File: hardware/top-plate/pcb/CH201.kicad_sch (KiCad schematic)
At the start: 35 parts

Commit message: some top plate changes
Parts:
- C10, C7, C8, C9: footprint PCM_Capacitor_SMD_AKL:C_1206_3216Metric_Pad1.33x1.80mm_HandSolder -> PCM_Capacitor_SMD_AKL:C_0805_2012Metric_Pad1.15x1.40mm_HandSolder
- R1, R2, R3, R7, R8: footprint PCM_Resistor_SMD_AKL:R_1206_3216Metric_Pad1.30x1.75mm_HandSolder -> PCM_Resistor_SMD_AKL:R_0805_2012Metric_Pad1.15x1.40mm_HandSolder
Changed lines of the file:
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@@
 			)
 		)
-		(property "Footprint" "PCM_Resistor_SMD_AKL:R_1206_3216Metric_Pad1.30x1.75mm_HandSolder"
+		(property "Footprint" "PCM_Resistor_SMD_AKL:R_0805_2012Metric_Pad1.15x1.40mm_HandSolder"
 			(at 264.922 207.01 90)
 			(effects
@@
 			)
 		)
-		(property "Footprint" "PCM_Resistor_SMD_AKL:R_1206_3216Metric_Pad1.30x1.75mm_HandSolder"
+		(property "Footprint" "PCM_Resistor_SMD_AKL:R_0805_2012Metric_Pad1.15x1.40mm_HandSolder"
 			(at 209.042 207.01 90)
 			(effects
@@
 			)
 		)
-		(property "Footprint" "PCM_Capacitor_SMD_AKL:C_1206_3216Metric_Pad1.33x1.80mm_HandSolder"
+		(property "Footprint" "PCM_Capacitor_SMD_AKL:C_0805_2012Metric_Pad1.15x1.40mm_HandSolder"
 			(at 224.79 200.9648 0)
 			(effects
@@
 			)
 		)
-		(property "Footprint" "PCM_Capacitor_SMD_AKL:C_1206_3216Metric_Pad1.33x1.80mm_HandSolder"
+		(property "Footprint" "PCM_Capacitor_SMD_AKL:C_0805_2012Metric_Pad1.15x1.40mm_HandSolder"
 			(at 240.03 200.9648 0)
 			(effects
@@
 			)
 		)
-		(property "Footprint" "PCM_Capacitor_SMD_AKL:C_1206_3216Metric_Pad1.33x1.80mm_HandSolder"
+		(property "Footprint" "PCM_Capacitor_SMD_AKL:C_0805_2012Metric_Pad1.15x1.40mm_HandSolder"
 			(at 280.67 200.9648 0)
 			(effects
@@
 	)
 	(symbol
+		(lib_name "MCP23S17_SO_1")
 		(lib_id "Interface_Expansion:MCP23S17_SO")
 		(at 260.35 71.12 0)
@@
 			)
 		)
-		(property "Footprint" "PCM_Capacitor_SMD_AKL:C_1206_3216Metric_Pad1.33x1.80mm_HandSolder"
+		(property "Footprint" "PCM_Capacitor_SMD_AKL:C_0805_2012Metric_Pad1.15x1.40mm_HandSolder"
 			(at 295.91 200.9648 0)
 			(effects
@@
 			)
 		)
-		(property "Footprint" "PCM_Resistor_SMD_AKL:R_1206_3216Metric_Pad1.30x1.75mm_HandSolder"
+		(property "Footprint" "PCM_Resistor_SMD_AKL:R_0805_2012Metric_Pad1.15x1.40mm_HandSolder"
 			(at 182.372 245.11 90)
 			(effects
@@
 			)
 		)
-		(property "Footprint" "PCM_Resistor_SMD_AKL:R_1206_3216Metric_Pad1.30x1.75mm_HandSolder"
+		(property "Footprint" "PCM_Resistor_SMD_AKL:R_0805_2012Metric_Pad1.15x1.40mm_HandSolder"
 			(at 202.692 245.11 90)
 			(effects
@@
 			)
 		)
-		(property "Footprint" "PCM_Resistor_SMD_AKL:R_1206_3216Metric_Pad1.30x1.75mm_HandSolder"
+		(property "Footprint" "PCM_Resistor_SMD_AKL:R_0805_2012Metric_Pad1.15x1.40mm_HandSolder"
 			(at 192.532 245.11 90)
 			(effects

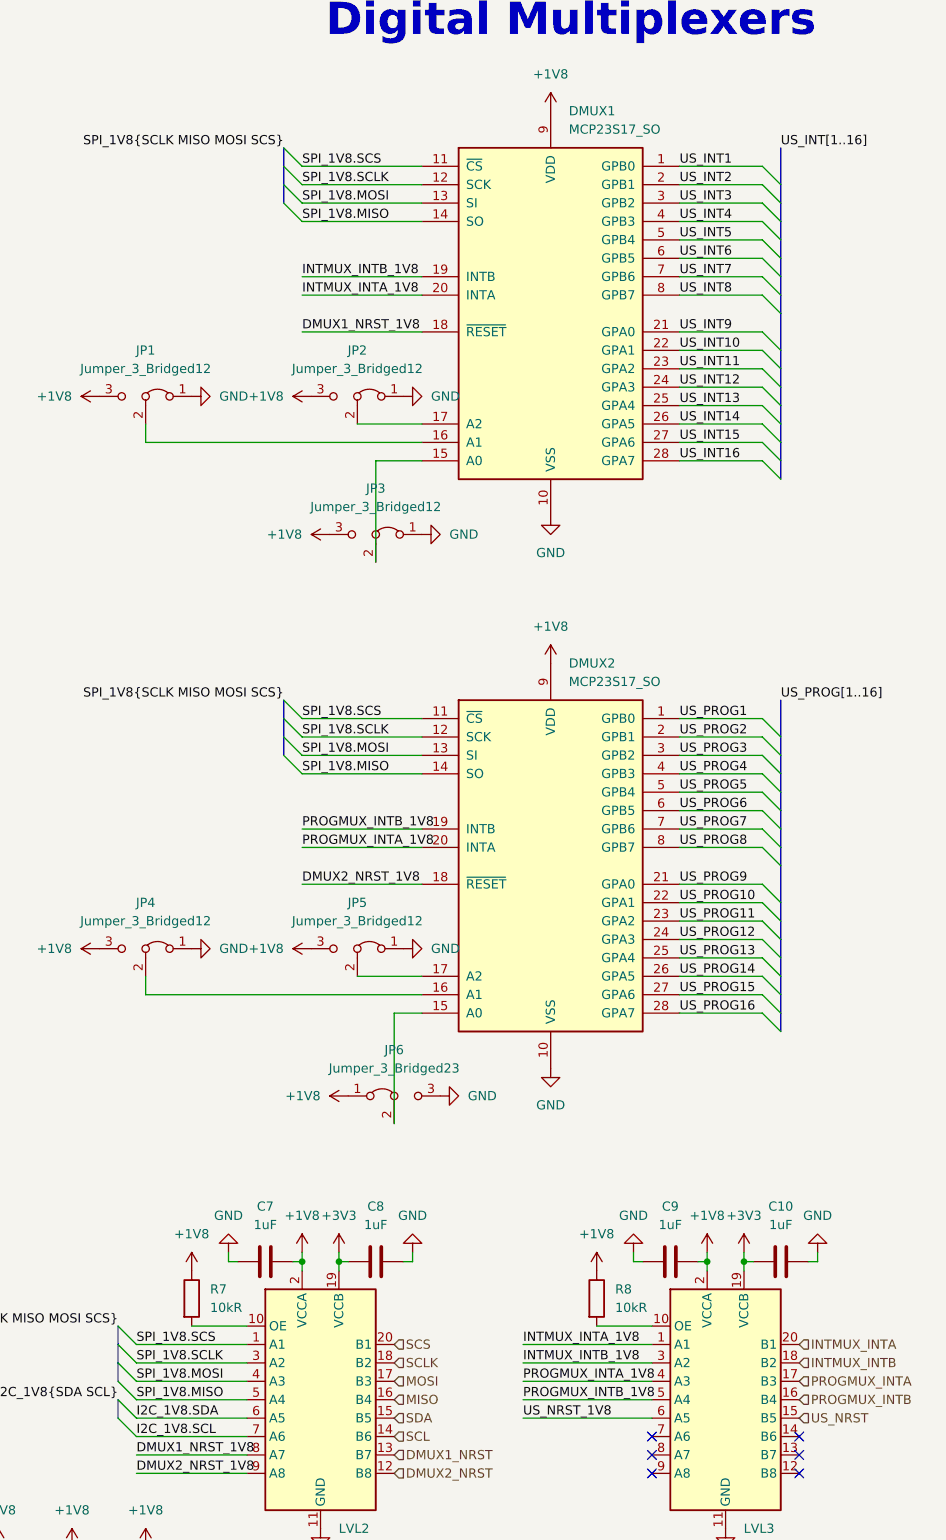
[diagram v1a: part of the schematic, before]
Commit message: fixed up bottom plate schematic. do not run a global symbol update! all modified symbols as of now are intentionally modified locally.
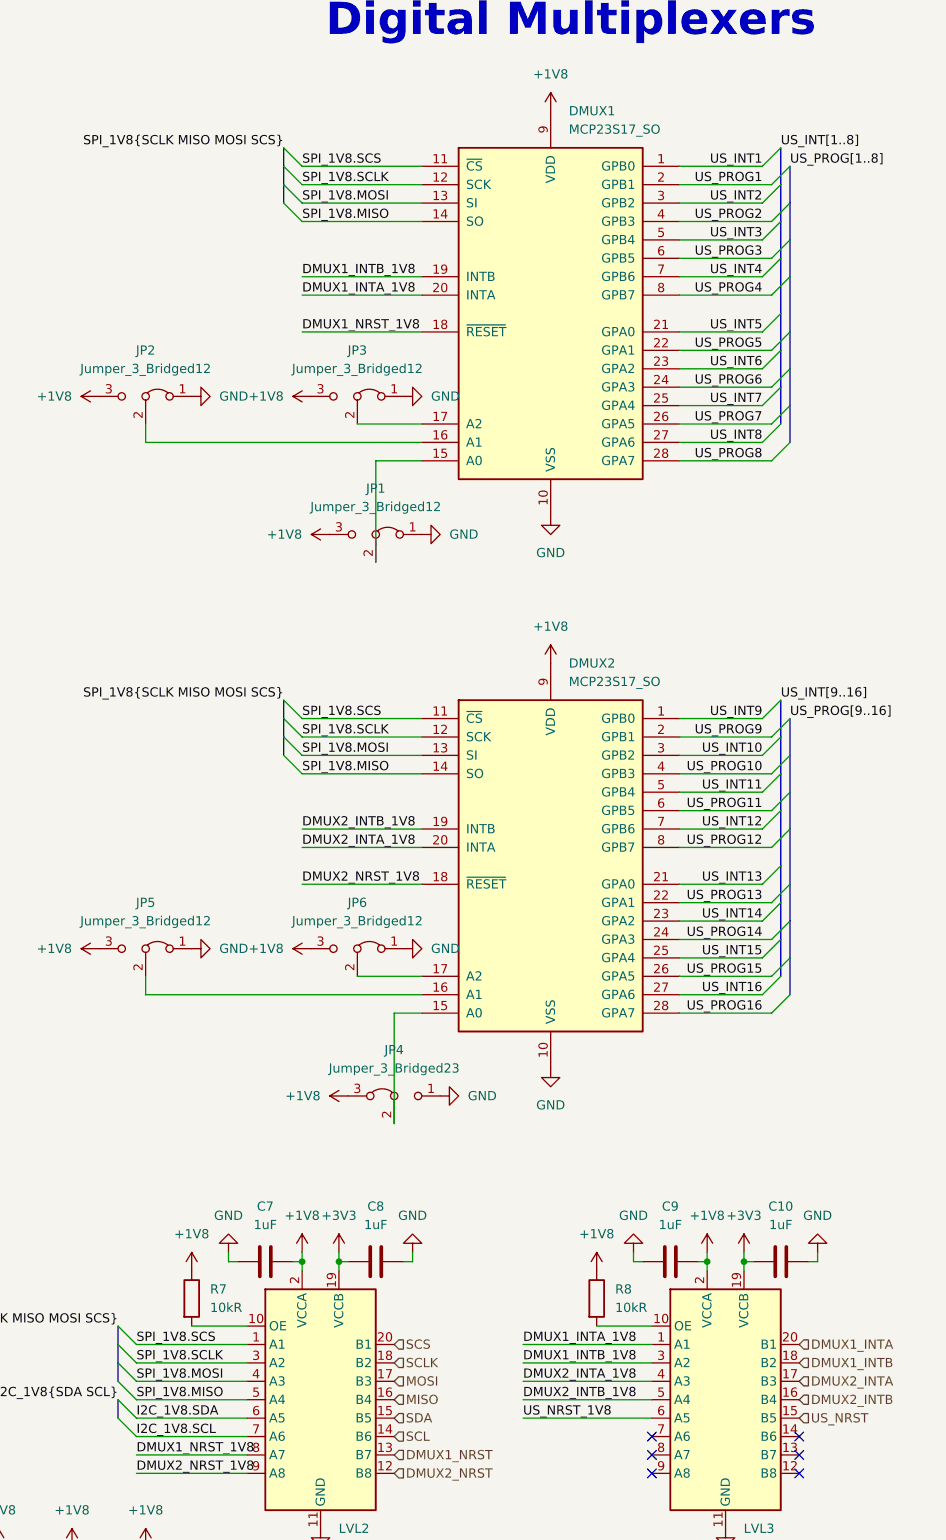
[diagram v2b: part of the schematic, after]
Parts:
- renumbered JP3 to JP1, JP1 to JP2, JP2 to JP3, JP6 to JP4, JP4 to JP5, JP5 to JP6
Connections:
- net +1V8: now also JP4.3 (A); no longer JP4.1 (A)
- net GND: now also JP4.1 (B); no longer JP4.3 (B)
- net US_INT10: now also DMUX2.3 (GPB2); no longer DMUX1.22 (GPA1)
- net US_INT11: now also DMUX2.5 (GPB4); no longer DMUX1.23 (GPA2)
- net US_INT12: now also DMUX2.7 (GPB6); no longer DMUX1.24 (GPA3)
- net US_INT13: now also DMUX2.21 (GPA0); no longer DMUX1.25 (GPA4)
- net US_INT14: now also DMUX2.23 (GPA2); no longer DMUX1.26 (GPA5)
- net US_INT15: now also DMUX2.25 (GPA4); no longer DMUX1.27 (GPA6)
- net US_INT16: now also DMUX2.27 (GPA6); no longer DMUX1.28 (GPA7)
- net US_INT2: now also DMUX1.3 (GPB2); no longer DMUX1.2 (GPB1)
- net US_INT3: now also DMUX1.5 (GPB4); no longer DMUX1.3 (GPB2)
- net US_INT4: now also DMUX1.7 (GPB6); no longer DMUX1.4 (GPB3)
- net US_INT5: now also DMUX1.21 (GPA0); no longer DMUX1.5 (GPB4)
- net US_INT6: now also DMUX1.23 (GPA2); no longer DMUX1.6 (GPB5)
- net US_INT7: now also DMUX1.25 (GPA4); no longer DMUX1.7 (GPB6)
- net US_INT8: now also DMUX1.27 (GPA6); no longer DMUX1.8 (GPB7)
- net US_INT9: now also DMUX2.1 (GPB0); no longer DMUX1.21 (GPA0)
- net US_PROG1: now also DMUX1.2 (GPB1); no longer DMUX2.1 (GPB0)
- net US_PROG10: now also DMUX2.4 (GPB3); no longer DMUX2.22 (GPA1)
- net US_PROG11: now also DMUX2.6 (GPB5); no longer DMUX2.23 (GPA2)
- net US_PROG12: now also DMUX2.8 (GPB7); no longer DMUX2.24 (GPA3)
- net US_PROG13: now also DMUX2.22 (GPA1); no longer DMUX2.25 (GPA4)
- net US_PROG14: now also DMUX2.24 (GPA3); no longer DMUX2.26 (GPA5)
- net US_PROG15: now also DMUX2.26 (GPA5); no longer DMUX2.27 (GPA6)
- net US_PROG2: now also DMUX1.4 (GPB3); no longer DMUX2.2 (GPB1)
- net US_PROG3: now also DMUX1.6 (GPB5); no longer DMUX2.3 (GPB2)
- net US_PROG4: now also DMUX1.8 (GPB7); no longer DMUX2.4 (GPB3)
- net US_PROG5: now also DMUX1.22 (GPA1); no longer DMUX2.5 (GPB4)
- net US_PROG6: now also DMUX1.24 (GPA3); no longer DMUX2.6 (GPB5)
- net US_PROG7: now also DMUX1.26 (GPA5); no longer DMUX2.7 (GPB6)
- net US_PROG8: now also DMUX1.28 (GPA7); no longer DMUX2.8 (GPB7)
- net US_PROG9: now also DMUX2.2 (GPB1); no longer DMUX2.21 (GPA0)
- net INTMUX_INTA renamed DMUX1_INTA
- net INTMUX_INTA_1V8 renamed DMUX1_INTA_1V8
- net INTMUX_INTB renamed DMUX1_INTB
- net INTMUX_INTB_1V8 renamed DMUX1_INTB_1V8
- net PROGMUX_INTA renamed DMUX2_INTA
- net PROGMUX_INTA_1V8 renamed DMUX2_INTA_1V8
- net PROGMUX_INTB renamed DMUX2_INTB
- net PROGMUX_INTB_1V8 renamed DMUX2_INTB_1V8

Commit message: top pcb completed
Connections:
- net DMUX1_INTB is gone; now on net SCL: LVL3.18 (B2)
- net DMUX2_INTB is gone; now on net MOSI: LVL3.16 (B4)
- net DMUX1_INTA: now also LVL2.20 (B1); no longer LVL3.20 (B1)
- net DMUX1_INTA_1V8: now also LVL2.1 (A1); no longer LVL3.1 (A1)
- net DMUX2_INTA: now also LVL3.13 (B7); no longer LVL3.17 (B3)
- net DMUX2_INTA_1V8: now also LVL3.8 (A7); no longer LVL3.4 (A3)
- net DMUX2_NRST: now also LVL3.12 (B8); no longer LVL2.12 (B8)
- net DMUX2_NRST_1V8: now also LVL3.9 (A8); no longer LVL2.9 (A8)
- net I2C_1V8.SCL: now also LVL3.3 (A2); no longer LVL2.7 (A6)
- net I2C_1V8.SDA: now also LVL3.1 (A1); no longer LVL2.6 (A5)
- net MISO: now also LVL2.17 (B3), LVL3.17 (B3); no longer LVL2.16 (B4)
- net MOSI: now also LVL2.16 (B4); no longer LVL2.17 (B3)
- net SCL: no longer LVL2.14 (B6)
- net SCLK: now also LVL2.15 (B5), LVL3.15 (B5); no longer LVL2.18 (B2)
- net SCS: now also LVL2.14 (B6), LVL3.14 (B6); no longer LVL2.20 (B1)
- net SDA: now also LVL3.20 (B1); no longer LVL2.15 (B5)
- net US_INT1: now also DMUX1.21 (GPA0); no longer DMUX1.1 (GPB0)
- net US_INT10: now also DMUX2.23 (GPA2); no longer DMUX2.3 (GPB2)
- net US_INT11: now also DMUX2.25 (GPA4); no longer DMUX2.5 (GPB4)
- net US_INT12: now also DMUX2.27 (GPA6); no longer DMUX2.7 (GPB6)
- net US_INT13: now also DMUX2.2 (GPB1); no longer DMUX2.21 (GPA0)
- net US_INT14: now also DMUX2.3 (GPB2); no longer DMUX2.23 (GPA2)
- net US_INT15: now also DMUX2.5 (GPB4); no longer DMUX2.25 (GPA4)
- net US_INT16: now also DMUX2.7 (GPB6); no longer DMUX2.27 (GPA6)
- net US_INT2: now also DMUX1.23 (GPA2); no longer DMUX1.3 (GPB2)
- net US_INT3: now also DMUX1.25 (GPA4); no longer DMUX1.5 (GPB4)
- net US_INT4: now also DMUX1.27 (GPA6); no longer DMUX1.7 (GPB6)
- net US_INT5: now also DMUX1.2 (GPB1); no longer DMUX1.21 (GPA0)
- net US_INT6: now also DMUX1.3 (GPB2); no longer DMUX1.23 (GPA2)
- net US_INT7: now also DMUX1.5 (GPB4); no longer DMUX1.25 (GPA4)
- net US_INT8: now also DMUX1.7 (GPB6); no longer DMUX1.27 (GPA6)
- net US_INT9: now also DMUX2.21 (GPA0); no longer DMUX2.1 (GPB0)
- net US_NRST: now also LVL2.18 (B2); no longer LVL3.15 (B5)
- net US_NRST_1V8: now also LVL2.3 (A2); no longer LVL3.6 (A5)
- net US_PROG1: now also DMUX1.22 (GPA1); no longer DMUX1.2 (GPB1)
- net US_PROG10: now also DMUX2.24 (GPA3); no longer DMUX2.4 (GPB3)
- net US_PROG11: now also DMUX2.26 (GPA5); no longer DMUX2.6 (GPB5)
- net US_PROG12: now also DMUX2.28 (GPA7); no longer DMUX2.8 (GPB7)
- net US_PROG13: now also DMUX2.1 (GPB0); no longer DMUX2.22 (GPA1)
- net US_PROG14: now also DMUX2.4 (GPB3); no longer DMUX2.24 (GPA3)
- net US_PROG15: now also DMUX2.6 (GPB5); no longer DMUX2.26 (GPA5)
- net US_PROG16: now also DMUX2.8 (GPB7); no longer DMUX2.28 (GPA7)
- net US_PROG2: now also DMUX1.24 (GPA3); no longer DMUX1.4 (GPB3)
- net US_PROG3: now also DMUX1.26 (GPA5); no longer DMUX1.6 (GPB5)
- net US_PROG4: now also DMUX1.28 (GPA7); no longer DMUX1.8 (GPB7)
- net US_PROG5: now also DMUX1.1 (GPB0); no longer DMUX1.22 (GPA1)
- net US_PROG6: now also DMUX1.4 (GPB3); no longer DMUX1.24 (GPA3)
- net US_PROG7: now also DMUX1.6 (GPB5); no longer DMUX1.26 (GPA5)
- net US_PROG8: now also DMUX1.8 (GPB7); no longer DMUX1.28 (GPA7)
- net US_PROG9: now also DMUX2.22 (GPA1); no longer DMUX2.2 (GPB1)
- net SPI_1V8_2.SCS: now reaches LVL3.7 (A6)
- net SPI_1V8_2.SCS: now also DMUX2.11 (~{CS})
- net DMUX1_INTB_1V8: no longer names the net of DMUX1.19 (INTB)
- net DMUX1_INTB_1V8: no longer LVL3.3 (A2)
- net DMUX2_INTB_1V8: no longer names the net of DMUX2.19 (INTB)
- net DMUX2_INTB_1V8: no longer LVL3.5 (A4)
- removed net SPI_1V8.MISO: DMUX1.14 (SO), DMUX2.14 (SO), LVL2.5 (A4)
- removed net SPI_1V8.MOSI: DMUX1.13 (SI), DMUX2.13 (SI), LVL2.4 (A3)
- removed net SPI_1V8.SCLK: DMUX1.12 (SCK), DMUX2.12 (SCK), LVL2.3 (A2)
- removed net SPI_1V8.SCS: DMUX1.11 (~{CS}), DMUX2.11 (~{CS}), LVL2.1 (A1)
- new net SPI_1V8_1.MISO: DMUX1.14 (SO), LVL2.4 (A3)
- new net SPI_1V8_1.MOSI: DMUX1.13 (SI), LVL2.5 (A4)
- new net SPI_1V8_1.SCLK: DMUX1.12 (SCK), LVL2.6 (A5)
- new net SPI_1V8_1.SCS: DMUX1.11 (~{CS}), LVL2.7 (A6)
- new net SPI_1V8_2.MISO: DMUX2.14 (SO), LVL3.4 (A3)
- new net SPI_1V8_2.MOSI: DMUX2.13 (SI), LVL3.5 (A4)
- new net SPI_1V8_2.SCLK: DMUX2.12 (SCK), LVL3.6 (A5)
- no-connect marks 38 -> 36
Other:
- moved on the sheet: C10, C9, LVL3, R8
